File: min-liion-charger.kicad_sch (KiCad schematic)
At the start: 12 parts, among them J1 Conn_01x02, J2 Conn_01x03, U1 bq21040

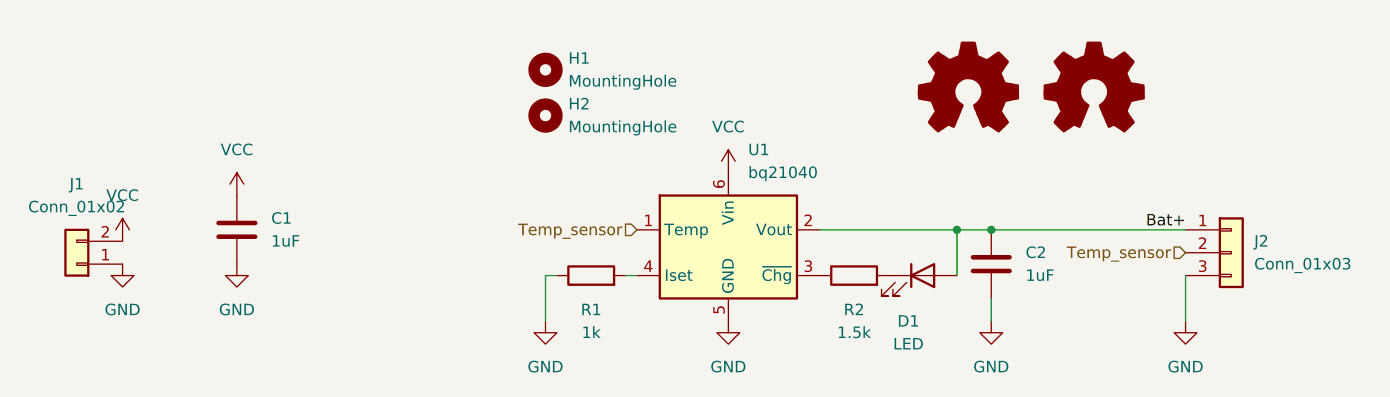
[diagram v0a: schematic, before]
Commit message: shrink, better silkscreen
Signed-off-by: Marcus Müller <marcus@hostalia.de>
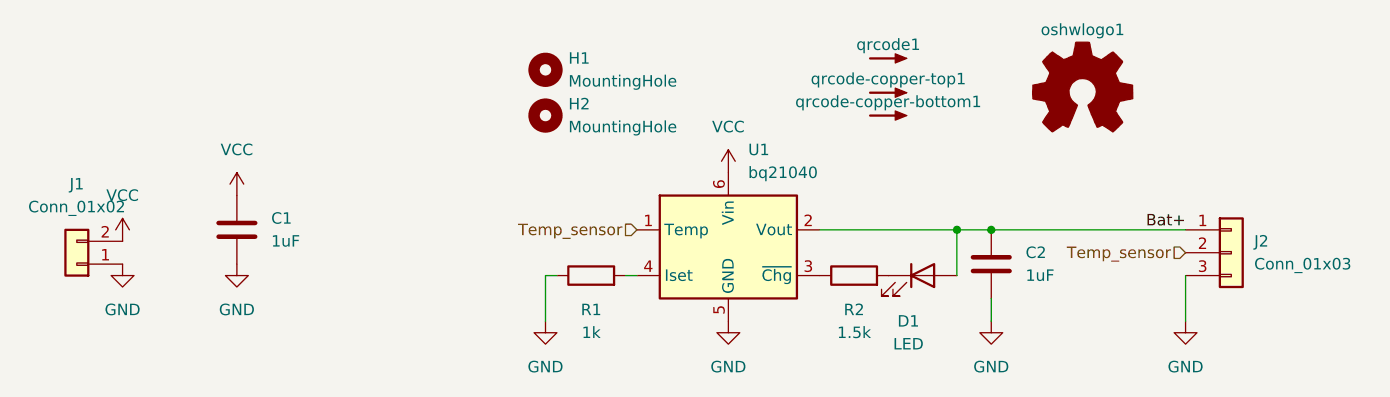
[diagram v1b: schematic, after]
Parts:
- removed SYM1: Logo_Open_Hardware_Small, Symbol:OSHW-Logo2_7.3x6mm_SilkScreen, symbol Graphic:Logo_Open_Hardware_Small
- removed SYM2: Logo_Open_Hardware_Small, Symbol:OSHW-Logo_5.7x6mm_Copper, symbol Graphic:Logo_Open_Hardware_Small
- added oshwlogo1: Logo_Open_Hardware_Small, Symbol:OSHW-Logo_5.7x6mm_SilkScreen, symbol Graphic:Logo_Open_Hardware_Small
- added qrcode-copper-bottom1, qrcode-copper-top1: SYM_Arrow_Small, QR:qr-copper, symbol Graphic:SYM_Arrow_Small
- added qrcode1: SYM_Arrow_Small, QR:QR code, symbol Graphic:SYM_Arrow_Small
- H1, H2: now left out of the parts list
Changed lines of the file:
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@@
+    )
+  )
+  (symbol (lib_id "Graphic:SYM_Arrow_Small") (at 130.81 82.55 0) (unit 1)
+    (in_bom no) (on_board yes) (dnp no) (fields_autoplaced)
+    (property "Reference" "qrcode-copper-top1" (at 130.81 81.026 0)
+      (effects (font (size 1.27 1.27)))
+    )
+    (property "Value" "SYM_Arrow_Small" (at 131.064 83.82 0)
+      (effects (font (size 1.27 1.27)) hide)
+    )
+    (property "Footprint" "QR:qr-copper" (at 130.81 82.55 0)
+      (effects (font (size 1.27 1.27)) hide)
+    )
+    (property "Datasheet" "~" (at 130.81 82.55 0)
+      (effects (font (size 1.27 1.27)) hide)
+    )
+    (property "Sim.Enable" "0" (at 130.81 82.55 0)
+      (effects (font (size 1.27 1.27)) hide)
+    )
+    (instances
+      (project "min-liion-charger"
+        (path "/88646ed8-be97-4917-8f8a-f8f60880150d"
+          (reference "qrcode-copper-top1") (unit 1)
+        )
+      )
     )
   )
@@
     )
   )
+  (symbol (lib_id "Graphic:SYM_Arrow_Small") (at 130.81 85.09 0) (unit 1)
+    (in_bom no) (on_board yes) (dnp no) (fields_autoplaced)
+    (property "Reference" "qrcode-copper-bottom1" (at 130.81 83.566 0)
+      (effects (font (size 1.27 1.27)))
+    )
+    (property "Value" "SYM_Arrow_Small" (at 131.064 86.36 0)
+      (effects (font (size 1.27 1.27)) hide)
+    )
+    (property "Footprint" "QR:qr-copper" (at 130.81 85.09 0)
+      (effects (font (size 1.27 1.27)) hide)
+    )
+    (property "Datasheet" "~" (at 130.81 85.09 0)
+      (effects (font (size 1.27 1.27)) hide)
+    )
+    (property "Sim.Enable" "0" (at 130.81 85.09 0)
+      (effects (font (size 1.27 1.27)) hide)
+    )
+    (instances
+      (project "min-liion-charger"
+        (path "/88646ed8-be97-4917-8f8a-f8f60880150d"
+          (reference "qrcode-copper-bottom1") (unit 1)
+        )
+      )
+    )
+  )
   (symbol (lib_id "Connector_Generic:Conn_01x03") (at 168.91 100.33 0) (unit 1)
     (in_bom yes) (on_board yes) (dnp no) (fields_autoplaced)
@@
   )
   (symbol (lib_id "Mechanical:MountingHole") (at 92.71 85.09 0) (unit 1)
-    (in_bom yes) (on_board yes) (dnp no) (fields_autoplaced)
+    (in_bom no) (on_board yes) (dnp no) (fields_autoplaced)
     (property "Reference" "H2" (at 95.25 83.82 0)
       (effects (font (size 1.27 1.27)) (justify left))
@@
     )
   )
-  (symbol (lib_id "Graphic:Logo_Open_Hardware_Small") (at 139.7 82.55 0) (unit 1)
-    (in_bom no) (on_board yes) (dnp no) (fields_autoplaced)
-    (property "Reference" "SYM1" (at 139.7 75.565 0)
-      (effects (font (size 1.27 1.27)) hide)
-    )
-    (property "Value" "Logo_Open_Hardware_Small" (at 139.7 88.265 0)
-      (effects (font (size 1.27 1.27)) hide)
-    )
-    (property "Footprint" "Symbol:OSHW-Logo2_7.3x6mm_SilkScreen" (at 139.7 82.55 0)
-      (effects (font (size 1.27 1.27)) hide)
-    )
-    (property "Datasheet" "~" (at 139.7 82.55 0)
-      (effects (font (size 1.27 1.27)) hide)
-    )
-    (property "Sim.Enable" "0" (at 139.7 82.55 0)
-      (effects (font (size 1.27 1.27)) hide)
-    )
-    (instances
-      (project "min-liion-charger"
-        (path "/88646ed8-be97-4917-8f8a-f8f60880150d"
-          (reference "SYM1") (unit 1)
-        )
-      )
-    )
-  )
   (symbol (lib_id "power:VCC") (at 58.42 93.98 0) (unit 1)
     (in_bom yes) (on_board yes) (dnp no) (fields_autoplaced)
@@
   )
   (symbol (lib_id "Mechanical:MountingHole") (at 92.71 80.01 0) (unit 1)
-    (in_bom yes) (on_board yes) (dnp no) (fields_autoplaced)
+    (in_bom no) (on_board yes) (dnp no) (fields_autoplaced)
     (property "Reference" "H1" (at 95.25 78.74 0)
       (effects (font (size 1.27 1.27)) (justify left))
@@
     )
   )
+  (symbol (lib_id "Graphic:Logo_Open_Hardware_Small") (at 152.4 82.55 0) (unit 1)
+    (in_bom no) (on_board yes) (dnp no) (fields_autoplaced)
+    (property "Reference" "oshwlogo1" (at 152.4 75.565 0)
+      (effects (font (size 1.27 1.27)))
+    )
+    (property "Value" "Logo_Open_Hardware_Small" (at 152.4 88.265 0)
+      (effects (font (size 1.27 1.27)) hide)
+    )
+    (property "Footprint" "Symbol:OSHW-Logo_5.7x6mm_SilkScreen" (at 152.4 82.55 0)
+      (effects (font (size 1.27 1.27)) hide)
+    )
+    (property "Datasheet" "~" (at 152.4 82.55 0)
+      (effects (font (size 1.27 1.27)) hide)
+    )
+    (property "Sim.Enable" "0" (at 152.4 82.55 0)
+      (effects (font (size 1.27 1.27)) hide)
+    )
+    (instances
+      (project "min-liion-charger"
+        (path "/88646ed8-be97-4917-8f8a-f8f60880150d"
+          (reference "oshwlogo1") (unit 1)
+        )
+      )
+    )
+  )
   (symbol (lib_id "Device:C") (at 142.24 101.6 0) (unit 1)
     (in_bom yes) (on_board yes) (dnp no) (fields_autoplaced)
@@
     )
   )
-  (symbol (lib_id "Graphic:Logo_Open_Hardware_Small") (at 153.67 82.55 0) (unit 1)
-    (in_bom no) (on_board yes) (dnp no) (fields_autoplaced)
-    (property "Reference" "SYM2" (at 153.67 75.565 0)
-      (effects (font (size 1.27 1.27)) hide)
-    )
-    (property "Value" "Logo_Open_Hardware_Small" (at 153.67 88.265 0)
-      (effects (font (size 1.27 1.27)) hide)
-    )
-    (property "Footprint" "Symbol:OSHW-Logo_5.7x6mm_Copper" (at 153.67 82.55 0)
-      (effects (font (size 1.27 1.27)) hide)
-    )
-    (property "Datasheet" "~" (at 153.67 82.55 0)
-      (effects (font (size 1.27 1.27)) hide)
-    )
-    (property "Sim.Enable" "0" (at 153.67 82.55 0)
-      (effects (font (size 1.27 1.27)) hide)
-    )
-    (instances
-      (project "min-liion-charger"
-        (path "/88646ed8-be97-4917-8f8a-f8f60880150d"
-          (reference "SYM2") (unit 1)
-        )
-      )
-    )
-  )
   (symbol (lib_id "power:VCC") (at 45.72 99.06 0) (unit 1)
     (in_bom yes) (on_board yes) (dnp no) (fields_autoplaced)
@@
         )
       )
+    )
+  )
+  (symbol (lib_id "Graphic:SYM_Arrow_Small") (at 130.81 78.74 0) (unit 1)
+    (in_bom no) (on_board yes) (dnp no) (fields_autoplaced)
+    (property "Reference" "qrcode1" (at 130.81 77.216 0)
+      (effects (font (size 1.27 1.27)))
+    )
+    (property "Value" "SYM_Arrow_Small" (at 131.064 80.01 0)
+      (effects (font (size 1.27 1.27)) hide)
+    )
+    (property "Footprint" "QR:QR code" (at 130.81 78.74 0)
+      (effects (font (size 1.27 1.27)) hide)
+    )
+    (property "Datasheet" "~" (at 130.81 78.74 0)
+      (effects (font (size 1.27 1.27)) hide)
+    )
+    (property "Sim.Enable" "0" (at 130.81 78.74 0)
+      (effects (font (size 1.27 1.27)) hide)
+    )
+    (instances
+      (project "min-liion-charger"
+        (path "/88646ed8-be97-4917-8f8a-f8f60880150d"
+          (reference "qrcode1") (unit 1)
+        )
+      )
